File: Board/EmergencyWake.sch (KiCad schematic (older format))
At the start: 124 parts, among them J1 USB_C_Plug_USB2.0, J2 Micro_SD_Card_Det, J3 Conn_01x03, J4 Conn_01x02, J5 Conn_01x03, J6 Conn_01x04, J7 Conn_01x02, J8 Conn_01x04, J9 Conn_01x04, Q1 AO3400A, Q2 AO3401A, SW1 SW_DPDT_x2, SW2 SW_Push, SW3 SW_Push, SW4 SW_Push, U1 M24C02-WMN, U10 L9110S, U2 AMS1117-3.3, U3 MC34063AD, U4 STM32F103VETx, U5 LM4670, U6 173950378, U7 PT6312B, U8 EL357N-G, U9 EL357N-G, Y1 32,768

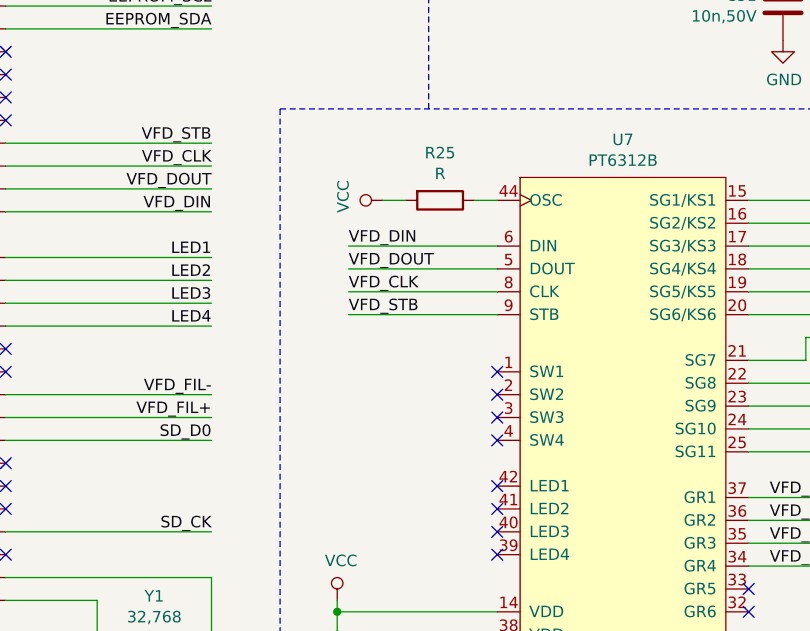
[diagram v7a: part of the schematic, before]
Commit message: [Board] Checked schematic for errors
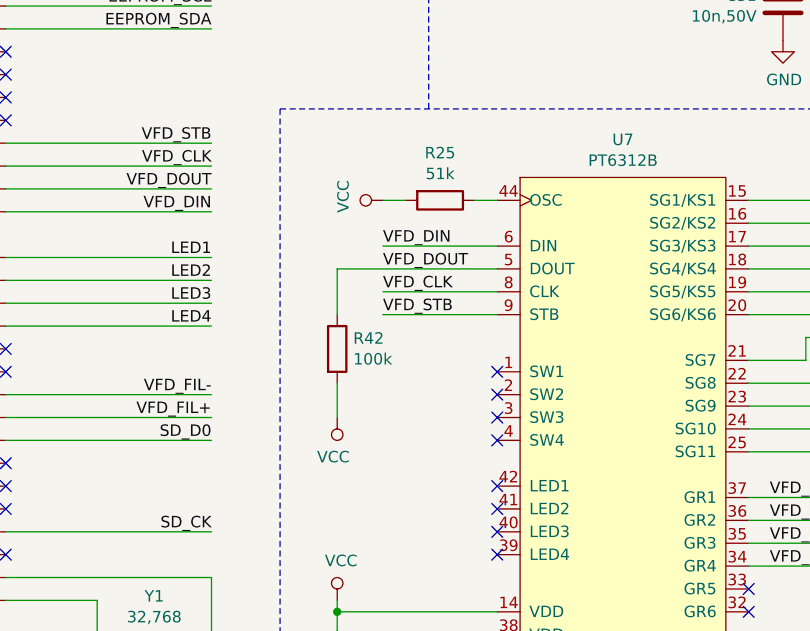
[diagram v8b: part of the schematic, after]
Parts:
- added R42: 100k, Resistor_SMD:R_0402_1005Metric, symbol Device:R
- C19, C20: LCSC (none) -> C57112
- R21, R22: LCSC (none) -> C23024
- R25: value R -> 51k; LCSC (none) -> C23196
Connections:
- net VCC: now also R42.2
- net VFD_DOUT: now also R42.1
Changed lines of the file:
@@
 	14450 6350 15050 6350
 Connection ~ 14450 6350
-Wire Wire Line
-	12250 7650 12900 7650
-Wire Wire Line
-	12250 7750 12900 7750
-Wire Wire Line
-	12250 7850 12900 7850
-Wire Wire Line
-	12250 7950 12900 7950
 Text Label 12900 7650 2    50   ~ 0
 VFD_GRID_1_HV
@@
 	1    0    0    -1
 $EndComp
-$Comp
-L power:-VDC #PWR041
-U 1 1 5E443986
-P 11150 8450
-F 0 "#PWR041" H 11150 8350 50  0001 C CNN
-F 1 "-VDC" H 11150 8725 50  0000 C CNN
-F 2 "" H 11150 8450 50  0001 C CNN
-F 3 "" H 11150 8450 50  0001 C CNN
-	1    11150 8450
-	0    -1   -1   0
-$EndComp
 Text Notes 8350 9700 0    50   ~ 0
 Negative supply for VFD\nSet to -19.63 V
@@
 	1    0    0    -1
 $EndComp
-Wire Wire Line
-	10450 8150 11150 8150
-Wire Wire Line
-	11150 8250 10450 8250
 Connection ~ 10450 8250
 Wire Wire Line
 	10450 8250 10450 8150
-Wire Wire Line
-	10450 8750 11150 8750
-Wire Wire Line
-	11150 8650 10450 8650
 Connection ~ 10450 8650
 Wire Wire Line
@@
 	10450 8750 10450 8900
 Connection ~ 10450 8750
-$Comp
-L VFD:PT6312B U7
-U 1 1 5F5EFE8A
-P 11700 8200
-F 0 "U7" H 11700 10315 50  0000 C CNN
-F 1 "PT6312B" H 11700 10224 50  0000 C CNN
-F 2 "Package_QFP:LQFP-44_10x10mm_P0.8mm" H 11700 10250 50  0001 C CNN
-F 3 "https://datasheet.lcsc.com/szlcsc/Princeton-Tech-PT6312B_C110225.pdf" H 11700 10250 50  0001 C CNN
-F 4 "C110225" H 11700 10250 50  0001 C CNN "LCSC"
-	1    11700 8200
-	1    0    0    -1
-$EndComp
-Wire Wire Line
-	12250 6350 13650 6350
-Wire Wire Line
-	12250 6450 13650 6450
-Wire Wire Line
-	12250 6550 13650 6550
-Wire Wire Line
-	12250 6650 13650 6650
 Wire Wire Line
 	13650 7150 12700 7150
@@
 	12700 7150 12700 7250
 Wire Wire Line
-	12700 7250 12250 7250
-Wire Wire Line
 	13650 7250 12800 7250
 Wire Wire Line
 	12800 7250 12800 7350
 Wire Wire Line
-	12800 7350 12250 7350
-Wire Wire Line
 	12900 7350 12900 7450
-Wire Wire Line
-	12900 7450 12250 7450
 Wire Wire Line
 	12900 7350 13650 7350
@@
 P 10900 6350
 F 0 "R25" V 10693 6350 50  0000 C CNN
-F 1 "R" V 10784 6350 50  0000 C CNN
+F 1 "51k" V 10784 6350 50  0000 C CNN
 F 2 "Resistor_SMD:R_0603_1608Metric" V 10830 6350 50  0001 C CNN
 F 3 "~" H 10900 6350 50  0001 C CNN
+F 4 "C23196" V 10900 6350 50  0001 C CNN "LCSC"
 	1    10900 6350
 	0    1    1    0
@@
 Wire Wire Line
 	10650 6350 10750 6350
-Wire Wire Line
-	11050 6350 11150 6350
-Wire Wire Line
-	11150 6550 10500 6550
-Wire Wire Line
-	11150 6650 10500 6650
-Wire Wire Line
-	11150 6750 10500 6750
-Wire Wire Line
-	11150 6850 10500 6850
-Text Label 10500 6550 0    50   ~ 0
+Text Label 10650 6550 0    50   ~ 0
 VFD_DIN
-Text Label 10500 6650 0    50   ~ 0
-VFD_DOUT
-Text Label 10500 6750 0    50   ~ 0
+Text Label 10650 6750 0    50   ~ 0
 VFD_CLK
-Text Label 10500 6850 0    50   ~ 0
+Text Label 10650 6850 0    50   ~ 0
 VFD_STB
-NoConn ~ 11150 7100
-NoConn ~ 11150 7300
-NoConn ~ 11150 7200
-NoConn ~ 11150 7400
-NoConn ~ 11150 7600
-NoConn ~ 11150 7700
-NoConn ~ 11150 7800
-NoConn ~ 11150 7900
-NoConn ~ 11550 9150
-NoConn ~ 11650 9150
-NoConn ~ 11750 9150
-NoConn ~ 11850 9150
-NoConn ~ 12250 8650
-NoConn ~ 12250 8550
-NoConn ~ 12250 8450
-NoConn ~ 12250 8150
-NoConn ~ 12250 8050
 $Comp
 L MCU_ST_STM32F1:STM32F103VETx U4
@@
 	1    0    0    -1
 $EndComp
-NoConn ~ 12250 8350
 $Comp
 L Connector:USB_C_Plug_USB2.0 J1
@@
 	-1   0    0    -1
 $EndComp
-$Comp
-L MotorDriver:L9110S U10
-U 1 1 5E4A70C0
-P 15150 9150
-F 0 "U10" H 15150 9665 50  0000 C CNN
-F 1 "L9110S" H 15150 9574 50  0000 C CNN
-F 2 "Package_SO:SOP-8_3.76x4.96mm_P1.27mm" H 15150 8550 50  0001 C CNN
-F 3 "https://datasheet.lcsc.com/szlcsc/Wuxi-Zhongwei-Aisin-Elec-L9110S_C85174.pdf" H 15150 8950 50  0001 C CNN
-F 4 "C85174" H 15150 8450 50  0001 C CNN "LCSC"
-	1    15150 9150
-	1    0    0    -1
-$EndComp
 Text Notes 13300 10300 0    50   ~ 0
 V_drive is 3.3 V\nabove -VDC
@@
 F 2 "Resistor_SMD:R_0603_1608Metric" V 9480 1450 50  0001 C CNN
 F 3 "~" H 9550 1450 50  0001 C CNN
+F 4 "C23024" V 9550 1450 50  0001 C CNN "LCSC"
 	1    9550 1450
 	0    -1   -1   0
@@
 F 2 "Resistor_SMD:R_0603_1608Metric" V 9230 1250 50  0001 C CNN
 F 3 "~" H 9300 1250 50  0001 C CNN
+F 4 "C23024" V 9300 1250 50  0001 C CNN "LCSC"
 	1    9300 1250
 	0    -1   -1   0
@@
 F 2 "Capacitor_SMD:C_0603_1608Metric" H 8988 1100 50  0001 C CNN
 F 3 "~" H 8950 1250 50  0001 C CNN
+F 4 "C57112" V 8950 1250 50  0001 C CNN "LCSC"
 	1    8950 1250
 	0    1    1    0
@@
 F 2 "Capacitor_SMD:C_0603_1608Metric" H 9288 1550 50  0001 C CNN
 F 3 "~" H 9250 1700 50  0001 C CNN
+F 4 "C57112" H 9250 1700 50  0001 C CNN "LCSC"
 	1    9250 1700
 	-1   0    0    1
@@
 	14350 7700 15800 7700
 Wire Wire Line
-	12250 6750 13650 6750
-Wire Wire Line
-	13650 6850 12250 6850
-Wire Wire Line
-	12250 7150 12600 7150
-Wire Wire Line
 	12600 7150 12600 7050
 Wire Wire Line
@@
 Wire Wire Line
 	12500 6950 12500 7050
-Wire Wire Line
-	12500 7050 12250 7050
 Text Label 13000 7450 0    50   ~ 0
 SEG_L
 Text Label 12900 8750 2    50   ~ 0
 SEG_L
-Wire Wire Line
-	12250 8750 12900 8750
 Wire Notes Line
 	10850 5950 10850 2300
@@
 Wire Wire Line
 	12400 3400 13700 3400
+$Comp
+L Device:R R42
+U 1 1 5E477866
+P 10450 7000
+F 0 "R42" H 10520 7046 50  0000 L CNN
+F 1 "100k" H 10520 6955 50  0000 L CNN
+F 2 "Resistor_SMD:R_0402_1005Metric" V 10380 7000 50  0001 C CNN
+F 3 "~" H 10450 7000 50  0001 C CNN
+F 4 "C25741" H 10450 7000 50  0001 C CNN "LCSC"
+	1    10450 7000
+	1    0    0    -1
+$EndComp
+$Comp
+L power:VCC #PWR0101
+U 1 1 5E678EA5
+P 10450 7300
+F 0 "#PWR0101" H 10450 7150 50  0001 C CNN
+F 1 "VCC" H 10467 7473 50  0000 C CNN
+F 2 "" H 10450 7300 50  0001 C CNN
+F 3 "" H 10450 7300 50  0001 C CNN
+	1    10450 7300
+	-1   0    0    1
+$EndComp
+Wire Wire Line
+	10450 7150 10450 7300
+Wire Wire Line
+	11150 6850 10650 6850
+Wire Wire Line
+	11150 6750 10650 6750
+Wire Wire Line
+	11150 8650 10450 8650
+Wire Wire Line
+	11150 6550 10650 6550
+Wire Wire Line
+	11050 6350 11150 6350
+Wire Wire Line
+	10450 8750 11150 8750
+NoConn ~ 11150 7600
+NoConn ~ 11150 7700
+NoConn ~ 11150 7800
+NoConn ~ 11150 7400
+NoConn ~ 11150 7900
+Wire Wire Line
+	11150 8250 10450 8250
+Wire Wire Line
+	12250 7650 12900 7650
+Wire Wire Line
+	12250 7750 12900 7750
+Wire Wire Line
+	12250 7850 12900 7850
+Wire Wire Line
+	12250 7950 12900 7950
+NoConn ~ 12250 8050
+NoConn ~ 12250 8150
+NoConn ~ 12250 8350
+NoConn ~ 12250 8450
+NoConn ~ 11150 7300
+NoConn ~ 12250 8550
+NoConn ~ 12250 8650
+$Comp
+L power:-VDC #PWR041
+U 1 1 5E443986
+P 11150 8450
+F 0 "#PWR041" H 11150 8350 50  0001 C CNN
+F 1 "-VDC" H 11150 8725 50  0000 C CNN
+F 2 "" H 11150 8450 50  0001 C CNN
+F 3 "" H 11150 8450 50  0001 C CNN
+	1    11150 8450
+	0    -1   -1   0
+$EndComp
+Wire Wire Line
+	12250 8750 12900 8750
+Wire Wire Line
+	12900 7450 12250 7450
+Wire Wire Line
+	12800 7350 12250 7350
+Wire Wire Line
+	12700 7250 12250 7250
+Wire Wire Line
+	12250 7150 12600 7150
+Wire Wire Line
+	12500 7050 12250 7050
+Wire Wire Line
+	13650 6850 12250 6850
+NoConn ~ 11150 7200
+Wire Wire Line
+	12250 6750 13650 6750
+Wire Wire Line
+	12250 6650 13650 6650
+Wire Wire Line
+	12250 6550 13650 6550
+Wire Wire Line
+	12250 6450 13650 6450
+Wire Wire Line
+	12250 6350 13650 6350
+Wire Wire Line
+	10450 8150 11150 8150
+NoConn ~ 11850 9150
+NoConn ~ 11750 9150
+NoConn ~ 11650 9150
+NoConn ~ 11550 9150
+NoConn ~ 11150 7100
+Wire Wire Line
+	10450 6650 10450 6850
+$Comp
+L VFD:PT6312B U7
+U 1 1 5F5EFE8A
+P 11700 8200
+F 0 "U7" H 11700 10315 50  0000 C CNN
+F 1 "PT6312B" H 11700 10224 50  0000 C CNN
+F 2 "Package_QFP:LQFP-44_10x10mm_P0.8mm" H 11700 10250 50  0001 C CNN
+F 3 "https://datasheet.lcsc.com/szlcsc/Princeton-Tech-PT6312B_C110225.pdf" H 11700 10250 50  0001 C CNN
+F 4 "C110225" H 11700 10250 50  0001 C CNN "LCSC"
+	1    11700 8200
+	1    0    0    -1
+$EndComp
+Wire Wire Line
+	10450 6650 11150 6650
+Text Label 10650 6650 0    50   ~ 0
+VFD_DOUT
+$Comp
+L MotorDriver:L9110S U10
+U 1 1 5E4A70C0
+P 15150 9150
+F 0 "U10" H 15150 9665 50  0000 C CNN
+F 1 "L9110S" H 15150 9574 50  0000 C CNN
+F 2 "Package_SO:SOP-8_3.76x4.96mm_P1.27mm" H 15150 8550 50  0001 C CNN
+F 3 "https://datasheet.lcsc.com/szlcsc/Wuxi-Zhongwei-Aisin-Elec-L9110S_C85174.pdf" H 15150 8950 50  0001 C CNN
+F 4 "C85174" H 15150 8450 50  0001 C CNN "LCSC"
+	1    15150 9150
+	1    0    0    -1
+$EndComp
 $EndSCHEMATC
